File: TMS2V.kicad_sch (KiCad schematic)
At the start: 1 part

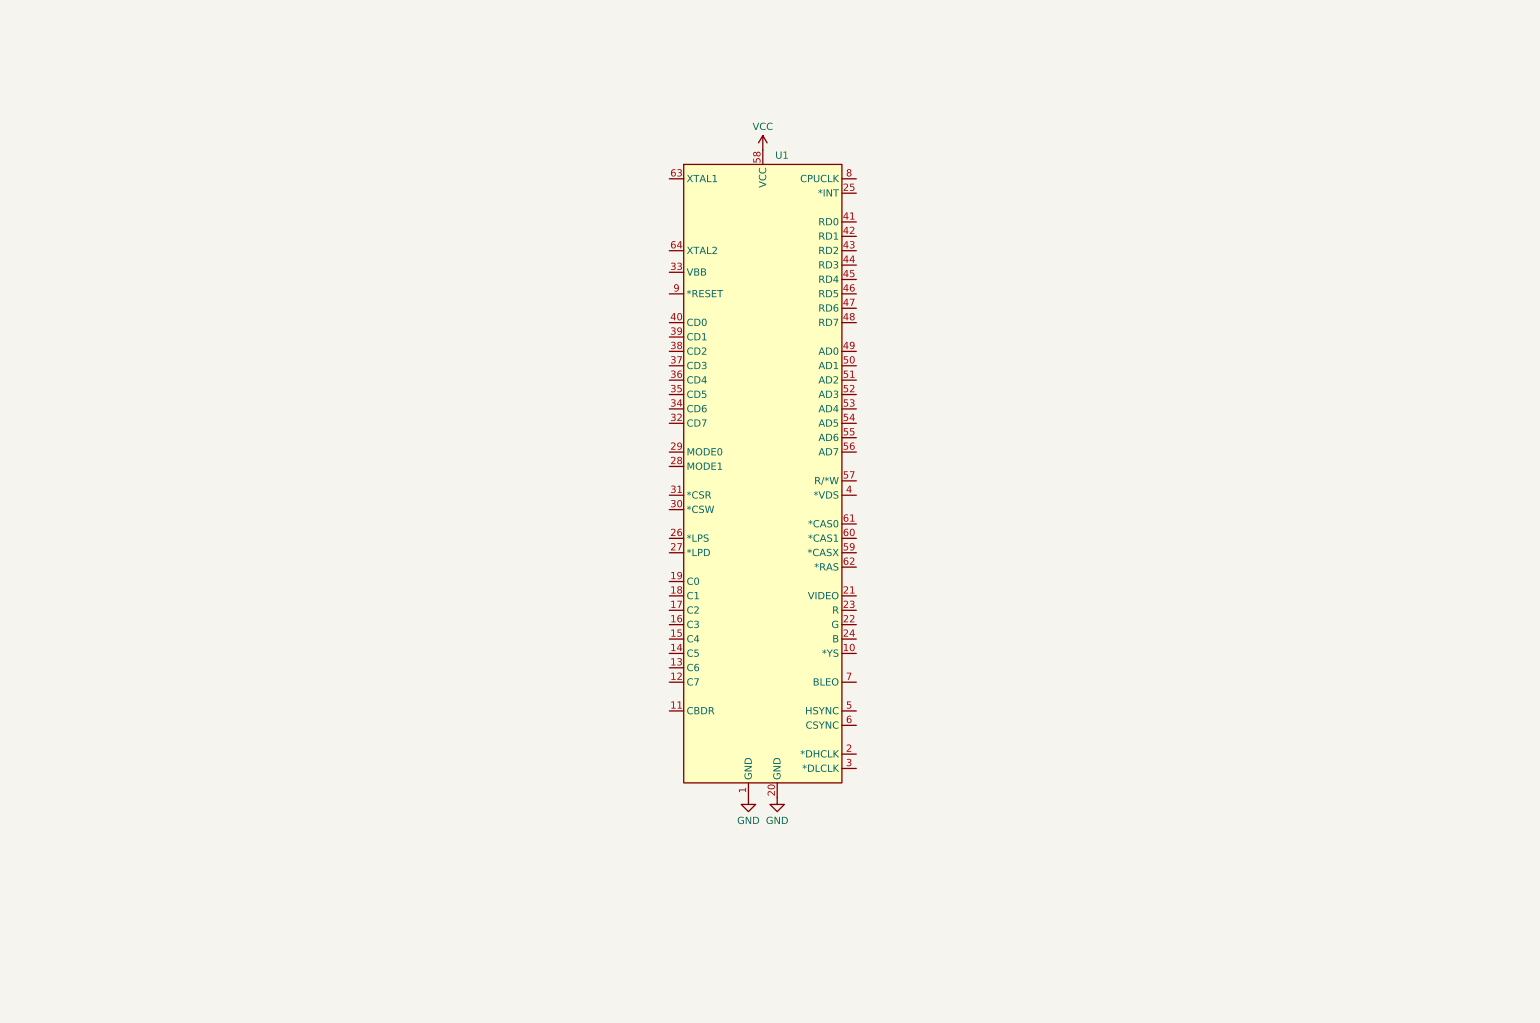
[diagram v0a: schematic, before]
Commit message: Added D41464 footprint and logic
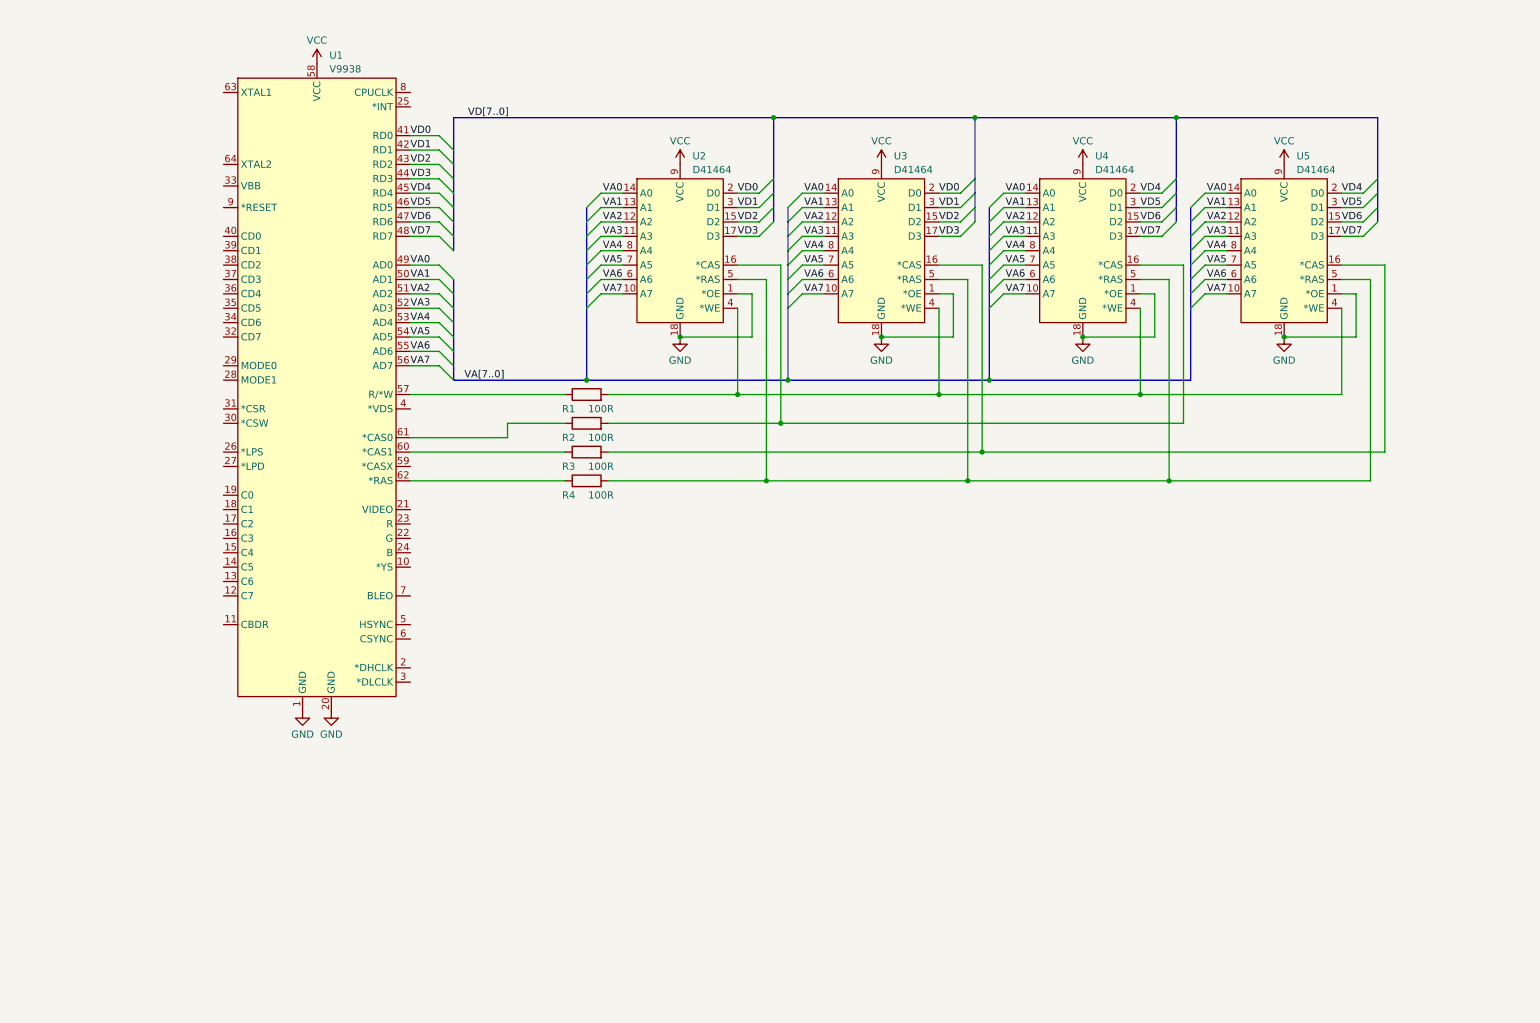
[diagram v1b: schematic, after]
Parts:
- added R1, R2, R3, R4: 100R, symbol Device:R
- added U2, U3, U4, U5: D41464, symbol Custom:D41464
- U1: value ~ -> V9938
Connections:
- net GND: now also U2.1 (*OE), U2.18 (GND), U3.1 (*OE), U3.18 (GND), U4.1 (*OE), U4.18 (GND), U5.1 (*OE), U5.18 (GND)
- net VCC: now also U2.9 (VCC), U3.9 (VCC), U4.9 (VCC), U5.9 (VCC)
- net VD0: now reaches U1.41 (RD0)
- net VD0: now also U2.2 (D0), U3.2 (D0)
- net VD1: now reaches U1.42 (RD1)
- net VD1: now also U2.3 (D1), U3.3 (D1)
- net VD2: now reaches U1.43 (RD2)
- net VD2: now also U2.15 (D2), U3.15 (D2)
- net VD3: now reaches U1.44 (RD3)
- net VD3: now also U2.17 (D3), U3.17 (D3)
- net VD4: now reaches U1.45 (RD4)
- net VD4: now also U4.2 (D0), U5.2 (D0)
- net VD5: now reaches U1.46 (RD5)
- net VD5: now also U4.3 (D1), U5.3 (D1)
- net VD6: now reaches U1.47 (RD6)
- net VD6: now also U4.15 (D2), U5.15 (D2)
- net VD7: now reaches U1.48 (RD7)
- net VD7: now also U4.17 (D3), U5.17 (D3)
- net VA0: now reaches U1.49 (AD0)
- net VA0: now also U2.14 (A0), U3.14 (A0), U4.14 (A0), U5.14 (A0)
- net VA1: now reaches U1.50 (AD1)
- net VA1: now also U2.13 (A1), U3.13 (A1), U4.13 (A1), U5.13 (A1)
- net VA2: now reaches U1.51 (AD2)
- net VA2: now also U2.12 (A2), U3.12 (A2), U4.12 (A2), U5.12 (A2)
- net VA3: now reaches U1.52 (AD3)
- net VA3: now also U2.11 (A3), U3.11 (A3), U4.11 (A3), U5.11 (A3)
- net VA4: now reaches U1.53 (AD4)
- net VA4: now also U2.8 (A4), U3.8 (A4), U4.8 (A4), U5.8 (A4)
- net VA5: now reaches U1.54 (AD5)
- net VA5: now also U2.7 (A5), U3.7 (A5), U4.7 (A5), U5.7 (A5)
- net VA6: now reaches U1.55 (AD6)
- net VA6: now also U2.6 (A6), U3.6 (A6), U4.6 (A6), U5.6 (A6)
- net VA7: now reaches U1.56 (AD7)
- net VA7: now also U2.10 (A7), U3.10 (A7), U4.10 (A7), U5.10 (A7)
- net at U1.57 (R/*W): now also R1.1
- net at U1.60 (*CAS1): now also R3.1
- net at U1.61 (*CAS0): now also R2.1
- net at U1.62 (*RAS): now also R4.1
- new net: R4.2, U2.5 (*RAS), U3.5 (*RAS), U4.5 (*RAS), U5.5 (*RAS)
- new net: R3.2, U3.16 (*CAS), U5.16 (*CAS)
- new net: R1.2, U2.4 (*WE), U3.4 (*WE), U4.4 (*WE), U5.4 (*WE)
- new net: R2.2, U2.16 (*CAS), U4.16 (*CAS)

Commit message: TMS9918A hookup
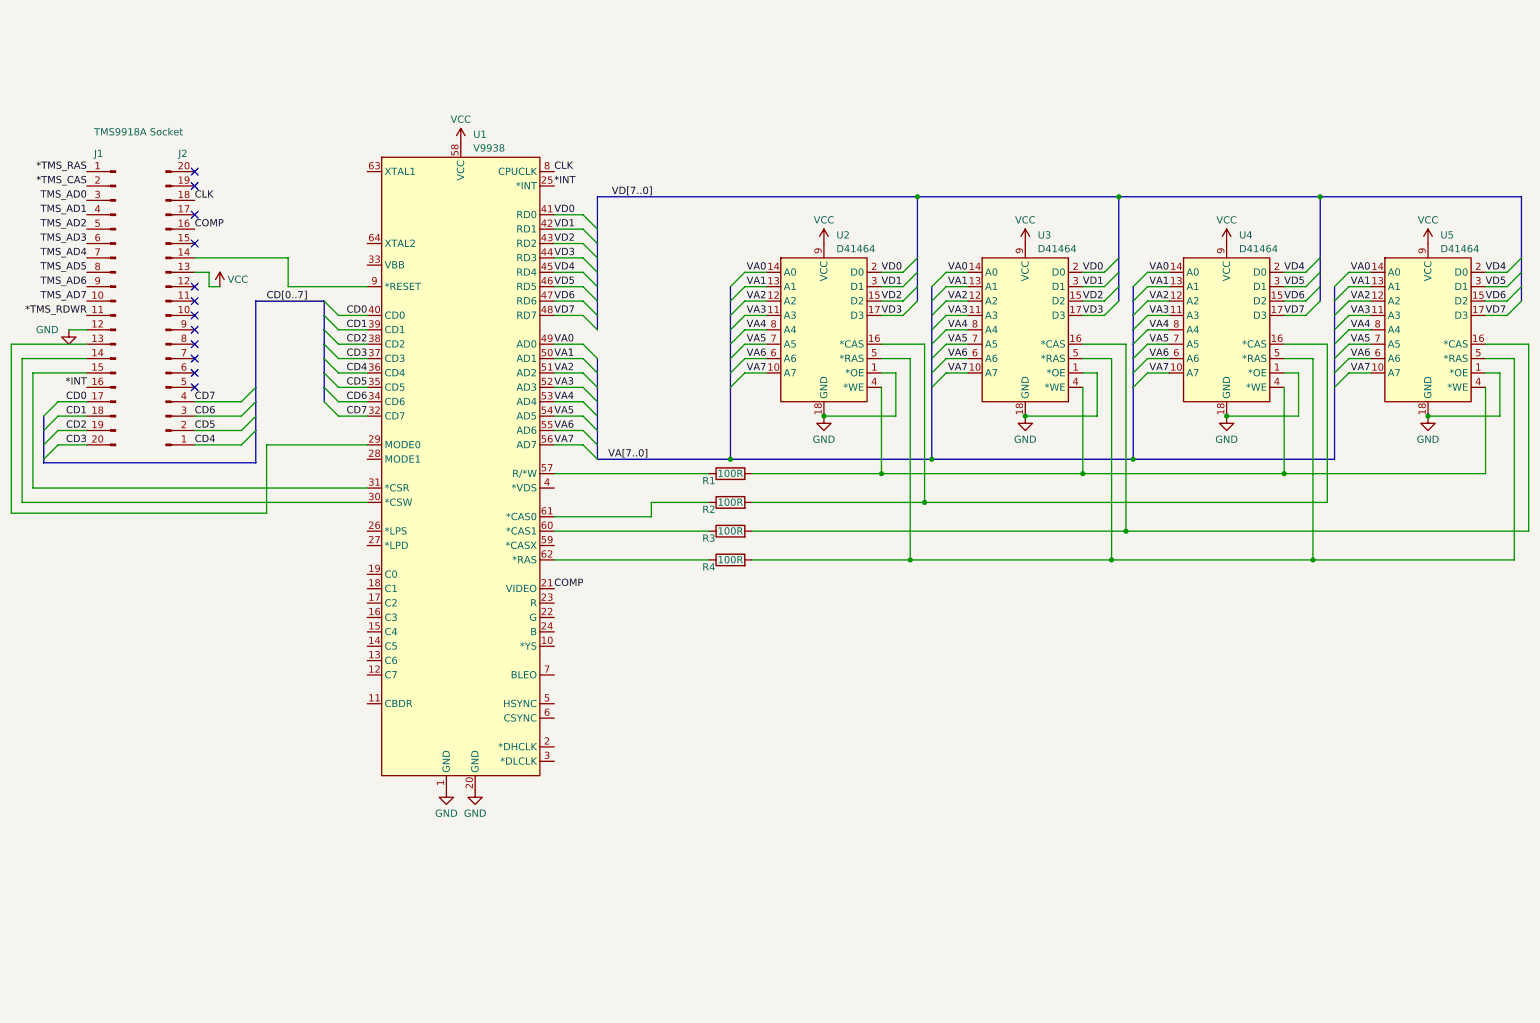
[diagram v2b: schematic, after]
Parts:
- added J1: TMS9918A Socket, symbol Connector:Conn_01x20_Pin
- added J2: ~, symbol Connector:Conn_01x20_Pin
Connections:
- net GND: now also J1.12 (Pin_12)
- net VCC: now also J2.13 (Pin_13)
- net COMP: now reaches U1.21 (VIDEO)
- net COMP: now also J2.16 (Pin_16)
- net *INT: now reaches U1.25 (*INT)
- net *INT: now also J1.16 (Pin_16)
- net at U1.29 (MODE0): now also J1.13 (Pin_13)
- net at U1.30 (*CSW): now also J1.14 (Pin_14)
- net at U1.31 (*CSR): now also J1.15 (Pin_15)
- net CD7: now reaches U1.32 (CD7)
- net CD7: now also J2.4 (Pin_4)
- net CD6: now reaches U1.34 (CD6)
- net CD6: now also J2.3 (Pin_3)
- net CD5: now reaches U1.35 (CD5)
- net CD5: now also J2.2 (Pin_2)
- net CD4: now reaches U1.36 (CD4)
- net CD4: now also J2.1 (Pin_1)
- net CD3: now reaches U1.37 (CD3)
- net CD3: now also J1.20 (Pin_20)
- net CD2: now reaches U1.38 (CD2)
- net CD2: now also J1.19 (Pin_19)
- net CD1: now reaches U1.39 (CD1)
- net CD1: now also J1.18 (Pin_18)
- net CD0: now reaches U1.40 (CD0)
- net CD0: now also J1.17 (Pin_17)
- net CLK: now reaches U1.8 (CPUCLK)
- net CLK: now also J2.18 (Pin_18)
- net at U1.9 (*RESET): now also J2.14 (Pin_14)
- new net *TMS_CAS: J1.2 (Pin_2)
- new net *TMS_RAS: J1.1 (Pin_1)
- new net *TMS_RDWR: J1.11 (Pin_11)
- new net TMS_AD0: J1.3 (Pin_3)
- new net TMS_AD1: J1.4 (Pin_4)
- new net TMS_AD2: J1.5 (Pin_5)
- new net TMS_AD3: J1.6 (Pin_6)
- new net TMS_AD4: J1.7 (Pin_7)
- new net TMS_AD5: J1.8 (Pin_8)
- new net TMS_AD6: J1.9 (Pin_9)
- new net TMS_AD7: J1.10 (Pin_10)
- no-connect marks 0 -> 12
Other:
- moved on the sheet: R1, R2, R3, R4, U1, U2, U3, U4, U5

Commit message: oscillator circuit
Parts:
- added C1: 0.1 uF, symbol Device:C_Small
- added C2: 33 Pf, symbol Device:C_Small
- added C3: 33 pF, symbol Device:C_Small
- added Y1: 24.47727 Mhz, symbol Device:Crystal
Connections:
- net GND: now also C1.1, C2.1, C3.1
- net at U1.33 (VBB): now also C1.2
- net at U1.63 (XTAL1): now also C2.2, Y1.2
- net at U1.64 (XTAL2): now also C3.2, Y1.1
- no-connect marks 12 -> 24

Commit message: Started work on video output circuit
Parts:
- added Q1, Q2, Q3, Q4: BC547, Package_TO_SOT_THT:TO-92_Inline, symbol Transistor_BJT:BC547
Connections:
- net VCC renamed +5V
- net +5V: now also Q1.1 (C), Q2.1 (C), Q3.1 (C), Q4.1 (C)
- no-connect marks 24 -> 28

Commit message: Started work on PCB layout
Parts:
- added C4, C5, C6, C7, C8: 0.1 uF, Capacitor_THT:C_Disc_D5.0mm_W2.5mm_P5.00mm, symbol Device:C_Small
- added J3: RGB Out, Custom:DIN-6, symbol Connector:DIN-6
- added J4: RGB Header, Connector_PinHeader_2.54mm:PinHeader_1x05_P2.54mm_Vertical, symbol Connector:Conn_01x05_Pin
- added JP1: Tie Mode 1, Connector_PinHeader_2.54mm:PinHeader_1x02_P2.54mm_Vertical, symbol Jumper:Jumper_2_Bridged
- added R10, R11, R12, R9: 220R, Resistor_THT:R_Axial_DIN0207_L6.3mm_D2.5mm_P7.62mm_Horizontal, symbol Device:R
- added R5, R6, R7, R8: 1K, Resistor_THT:R_Axial_DIN0207_L6.3mm_D2.5mm_P7.62mm_Horizontal, symbol Device:R
- added RN1, RN2: 10K, Resistor_THT:R_Array_SIP9, symbol Device:R_Network08
- C1, C2, C3: footprint (none) -> Capacitor_THT:C_Disc_D5.0mm_W2.5mm_P5.00mm
- J1, J2: footprint (none) -> Connector_PinHeader_2.54mm:PinHeader_1x20_P2.54mm_Vertical
- R1, R2, R3, R4: footprint (none) -> Resistor_THT:R_Axial_DIN0207_L6.3mm_D2.5mm_P7.62mm_Horizontal
- U1: footprint (none) -> Custom:DIP64
- U2, U3, U4, U5: footprint (none) -> Package_DIP:DIP-18_W7.62mm
- Y1: footprint (none) -> Crystal:Crystal_HC49-U_Vertical
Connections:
- net *TMS_CAS: now also RN2.7 (R6)
- net *TMS_RAS: now also RN2.6 (R5)
- net *TMS_RDWR: now also RN2.5 (R4)
- net +5V: now also C4.1, C5.1, C6.1, C7.1, C8.1, RN1.1 (common), RN2.1 (common)
- net GND: now also C4.2, C5.2, C6.2, C7.2, C8.2, J3.3, J4.5 (Pin_5), JP1.1 (A), R10.1, R11.1, R12.1, R6.1, R7.1, R8.1, R9.1
- net TMS_AD0: now also RN1.2 (R1)
- net TMS_AD1: now also RN1.3 (R2)
- net TMS_AD2: now also RN1.4 (R3)
- net TMS_AD3: now also RN1.5 (R4)
- net TMS_AD4: now also RN1.6 (R5)
- net TMS_AD5: now also RN1.7 (R6)
- net TMS_AD6: now also RN1.8 (R7)
- net TMS_AD7: now also RN1.9 (R8)
- net at Q4.2 (B): now also R5.2
- net CSYNC: now reaches Q4.3 (E)
- net CSYNC: now also J3.6, J4.4 (Pin_4), R9.2
- net at Q1.2 (B): now also U1.23 (R), R8.2
- net RED: now reaches Q1.3 (E)
- net RED: now also J3.4, J4.1 (Pin_1), R12.2
- net at Q3.2 (B): now also U1.24 (B), R6.2
- net BLUE: now reaches Q3.3 (E)
- net BLUE: now also J3.5, J4.3 (Pin_3), R10.2
- net at U1.22 (G): now also Q2.2 (B), R7.2
- net at U1.26 (*LPS): now also RN2.9 (R8)
- net at U1.27 (*LPD): now also RN2.8 (R7)
- net at U1.28 (MODE1): now also JP1.2 (B)
- net at U1.6 (CSYNC): now also R5.1
- net GREEN: now reaches Q2.3 (E)
- net GREEN: now also J3.1, J4.2 (Pin_2), R11.2
- no-connect marks 28 -> 32
